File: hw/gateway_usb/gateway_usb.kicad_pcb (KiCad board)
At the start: 2 copper layers, 68 x 68 mm, 47 parts, among them J1 GCT Micro USB 2.0 Type B vert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, U1 6MHz, U2 FT2232D, U3 ADuM1201, U4 ADuM1201, U5 ADuM1201, U6 ADuM1201

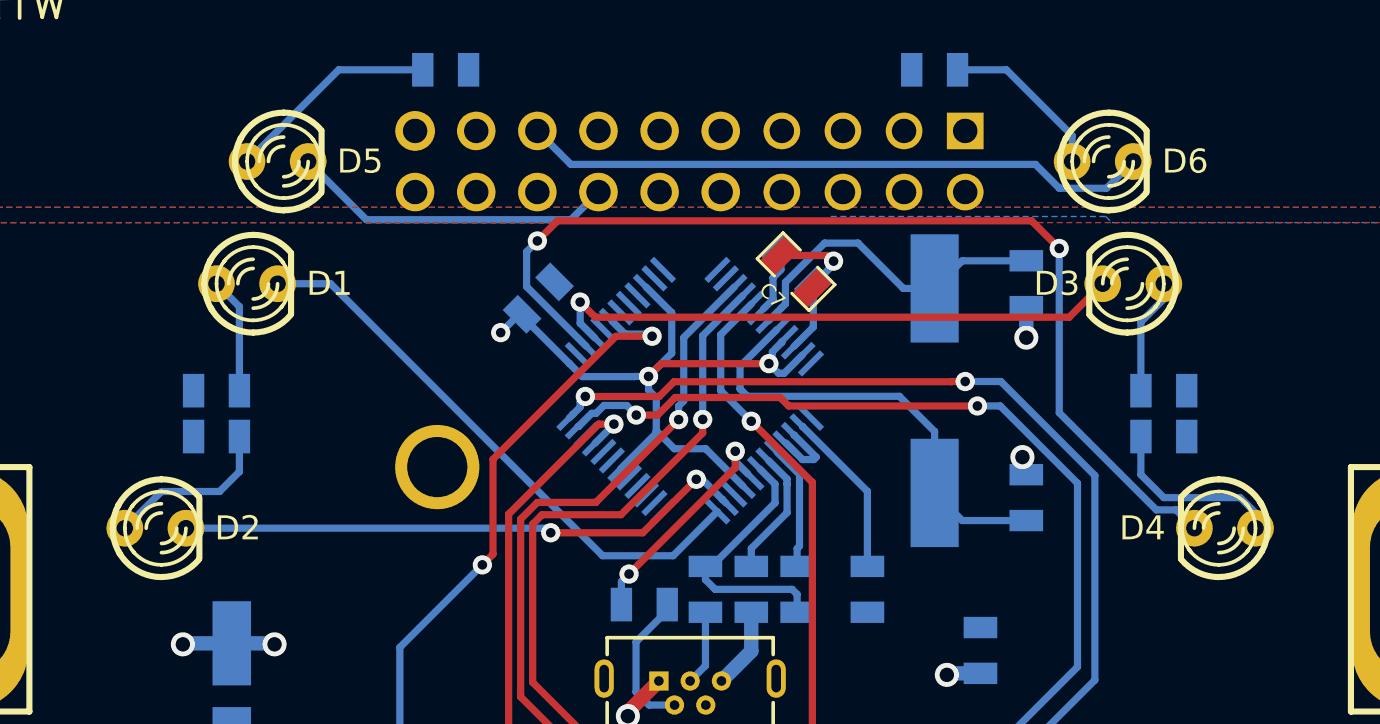
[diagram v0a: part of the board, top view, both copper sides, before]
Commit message: Update to KiCAD6: gateway_usb
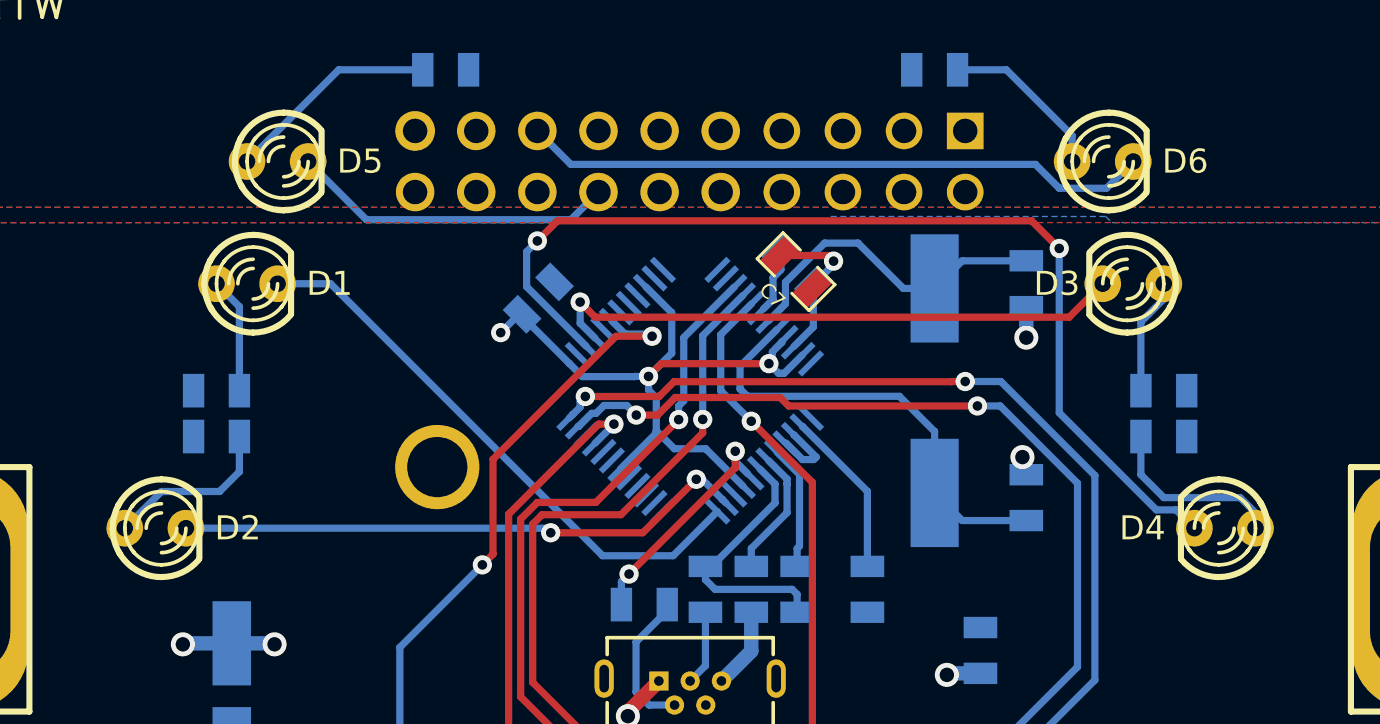
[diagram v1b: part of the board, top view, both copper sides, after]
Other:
- net class Default removed
- net class Power removed
